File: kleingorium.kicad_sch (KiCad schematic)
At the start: 47 parts, among them J1 4017 Pins, J10 VCC, J11 GND, J12 4046 Comp In, J13 Select, J14 Input, J15 4046 SigIn, J16 4046 Comp, J17 Output, J18 4046 Comp In, J19 4046 Out, J2 4040 Output, J20 4040 Input, J21 4040 Output, J22 4017 Pins, J23 VCC, J24 GND, J3 4040 Input, J4 4046 Out, J5 4046 Comp, J6 Select, J7 Output, J8 Input, J9 4046 SigIn, Q1 2N3904, Q2 2N3904, Q3 2N3904, Q4 2N3904, Q5 2N3904, Q6 2N3904, SW1 4017 Feedback, SW2 4046 CompIn, SW3 Chain, SW4 4017 Feedback, SW5 4046 CompIn

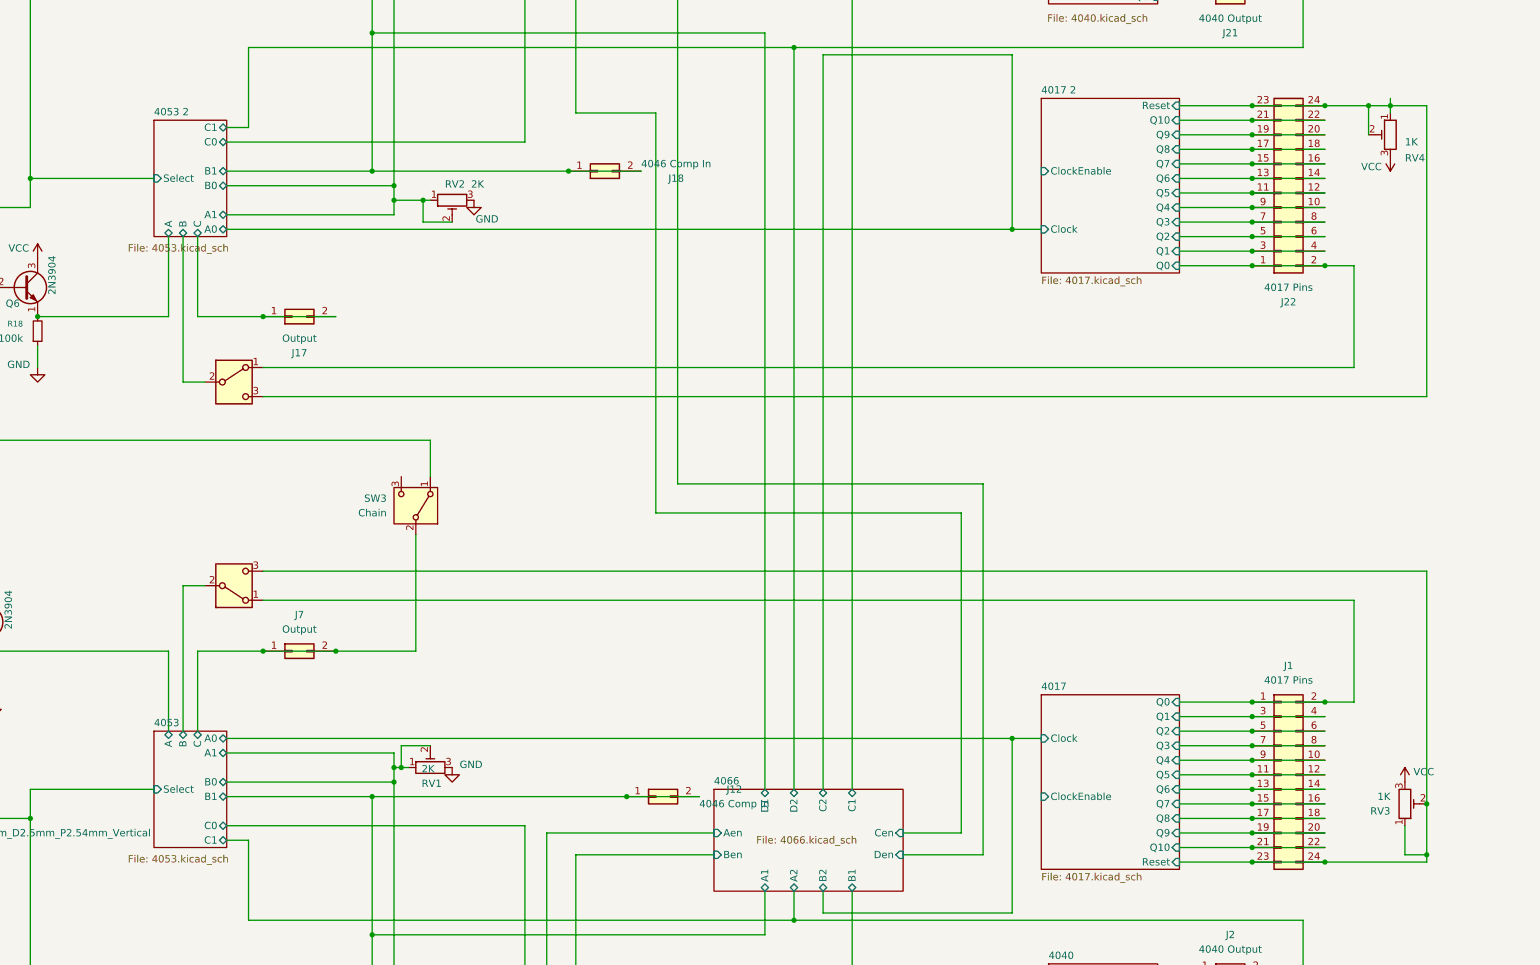
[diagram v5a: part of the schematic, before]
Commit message: add Inhibit 4046
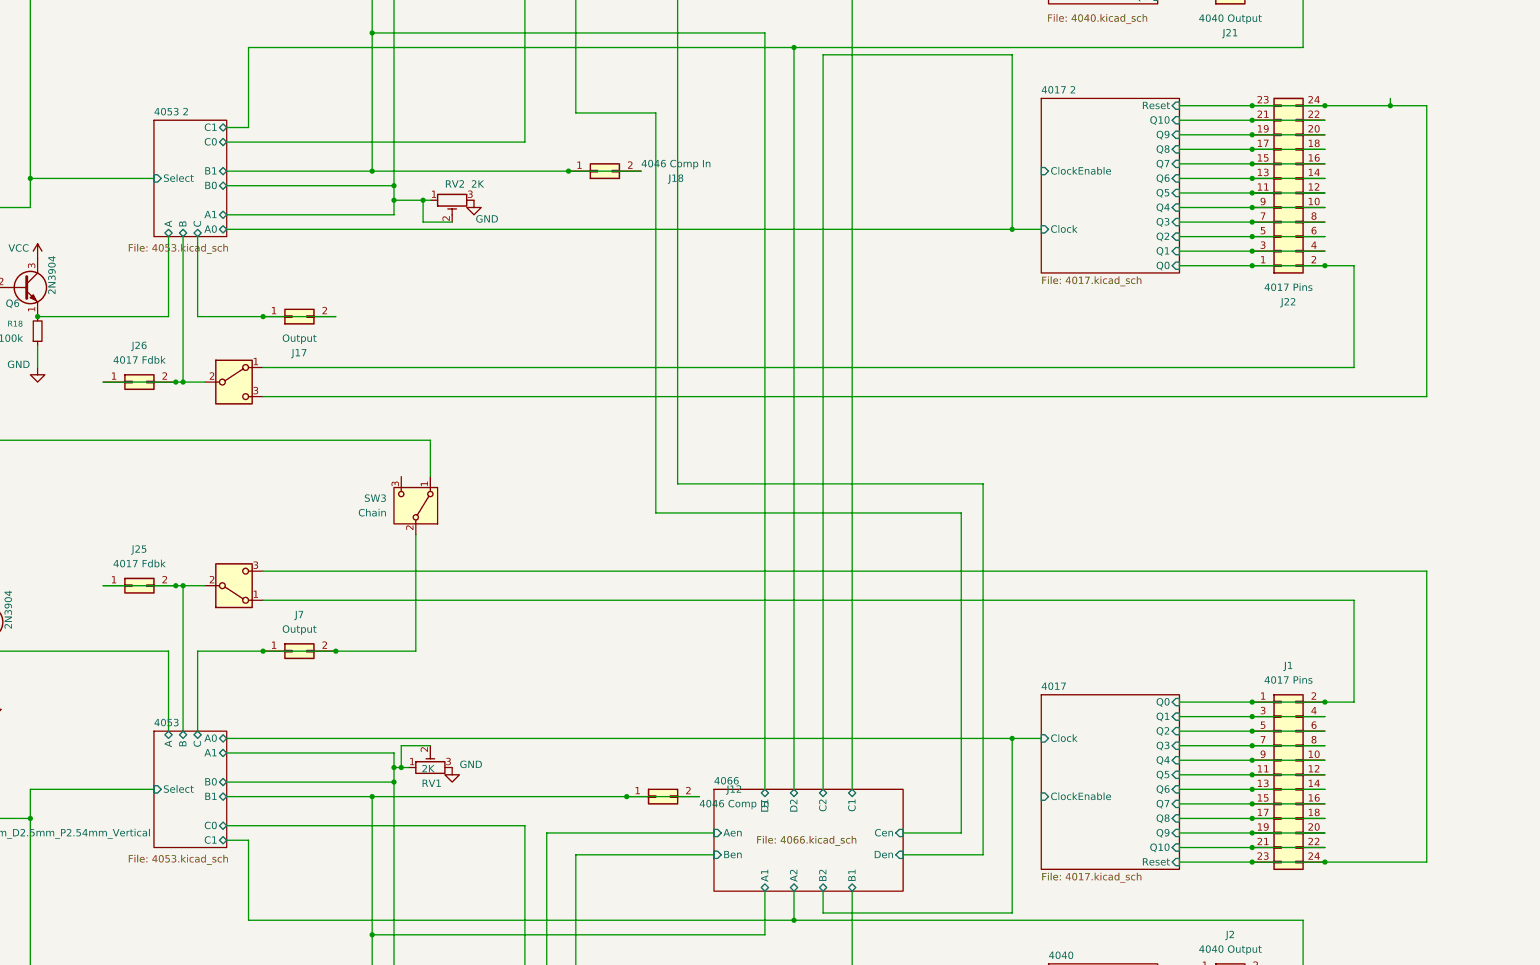
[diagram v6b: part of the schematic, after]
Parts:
- removed RV3, RV4: 1K, Potentiometer_THT:Potentiometer_Bourns_3296W_Vertical, symbol Device:R_Potentiometer_Trim
- added J25, J26: 4017 Fdbk, Connector_PinHeader_2.54mm:PinHeader_2x01_P2.54mm_Vertical, symbol Connector_Generic:Conn_02x01
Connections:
- net 4053 2/B: now also J26.1 (Pin_1), J26.2 (Pin_2)
- net 4053/B: now also J25.1 (Pin_1), J25.2 (Pin_2)

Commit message: v2 initial commit
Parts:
- removed J1, J22: 4017 Pins, Connector_PinHeader_2.54mm:PinHeader_2x12_P2.54mm_Vertical, symbol Connector_Generic:Conn_02x12_Odd_Even
- removed J12, J18: 4046 Comp In, Connector_PinHeader_2.54mm:PinHeader_2x01_P2.54mm_Vertical, symbol Connector_Generic:Conn_02x01
- removed J13, J6: Select, Connector_PinHeader_2.54mm:PinHeader_2x01_P2.54mm_Vertical, symbol Connector_Generic:Conn_02x01
- removed J14, J8: Input, Connector_PinHeader_2.54mm:PinHeader_2x01_P2.54mm_Vertical, symbol Connector_Generic:Conn_02x01
- removed J15, J9: 4046 SigIn, Connector_PinHeader_2.54mm:PinHeader_2x01_P2.54mm_Vertical, symbol Connector_Generic:Conn_02x01
- removed J16, J5: 4046 Comp, Connector_PinHeader_2.54mm:PinHeader_2x01_P2.54mm_Vertical, symbol Connector_Generic:Conn_02x01
- removed J17, J7: Output, Connector_PinHeader_2.54mm:PinHeader_2x01_P2.54mm_Vertical, symbol Connector_Generic:Conn_02x01
- removed J19, J4: 4046 Out, Connector_PinHeader_2.54mm:PinHeader_2x01_P2.54mm_Vertical, symbol Connector_Generic:Conn_02x01
- removed J2, J21: 4040 Output, Connector_PinHeader_2.54mm:PinHeader_2x12_P2.54mm_Vertical, symbol Connector_Generic:Conn_02x12_Odd_Even
- removed J20, J3: 4040 Input, Connector_PinHeader_2.54mm:PinHeader_1x02_P2.54mm_Vertical, symbol Connector_Generic:Conn_01x02
- removed J25, J26: 4017 Fdbk, Connector_PinHeader_2.54mm:PinHeader_2x01_P2.54mm_Vertical, symbol Connector_Generic:Conn_02x01
- removed Q1, Q2, Q3, Q4, Q5, Q6: 2N3904, Package_TO_SOT_THT:TO-92_Inline_Wide, symbol Transistor_BJT:2N3904
- removed R11, R14: 2.2k, Resistor_THT:R_Axial_DIN0207_L6.3mm_D2.5mm_P10.16mm_Horizontal, symbol Device:R_Small
- removed R12, R13: 100k, Resistor_THT:R_Axial_DIN0207_L6.3mm_D2.5mm_P10.16mm_Horizontal, symbol Device:R_Small
- removed R15, R16, R17, R18: 100k, Resistor_THT:R_Axial_DIN0207_L6.3mm_D2.5mm_P2.54mm_Vertical, symbol Device:R_Small
- removed RV1, RV2: 2K, Potentiometer_THT:Potentiometer_Bourns_3296W_Vertical, symbol Device:R_Potentiometer_Trim
- removed SW1, SW4: 4017 Feedback, Button_Switch_THT:SW_CK_JS202011CQN_DPDT_Straight, symbol Switch:SW_DPDT_x2
- removed SW2, SW5: 4046 CompIn, Button_Switch_THT:SW_E-Switch_EG1271_SPDT, symbol Switch:SW_SPDT
- removed SW3: Chain, Button_Switch_THT:SW_E-Switch_EG1271_SPDT, symbol Switch:SW_SPDT
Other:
- removed sheet 4017
- removed sheet 4017 2
- removed sheet 4040
- removed sheet 4040 2
- removed sheet 4046
- removed sheet 4046 2
- removed sheet 4053
- removed sheet 4053 2
- removed sheet 4066
- added sheet Multiplier-Divider (multiplier_divider.kicad_sch)

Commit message: schematic finished
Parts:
- renumbered J10 to J1, J23 to J2, J11 to J3, J24 to J4
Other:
- removed sheet utilities
- added sheet Bottom plate (bottom_plate.kicad_sch)
- added sheet Top Plate (top_plate.kicad_sch)
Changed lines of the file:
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@@
 	(paper "A3")
 	(junction
-		(at 370.84 185.42)
-		(diameter 0)
-		(color 0 0 0 0)
-	)
-	(junction
 		(at 386.08 182.88)
 		(diameter 0)
@@
 	)
 	(junction
-		(at 386.08 185.42)
+		(at 400.05 182.88)
+		(diameter 0)
+		(color 0 0 0 0)
+	)
+	(junction
+		(at 387.35 182.88)
+		(diameter 0)
+		(color 0 0 0 0)
+	)
+	(junction
+		(at 387.35 199.39)
 		(diameter 0)
 		(color 0 0 0 0)
@@
 	(wire
 		(pts
-			(xy 386.08 182.88) (xy 386.08 185.42)
-		)
-		(stroke
-			(width 0)
-			(type default)
-		)
-	)
-	(wire
-		(pts
-			(xy 400.05 201.93) (xy 386.08 201.93)
+			(xy 387.35 199.39) (xy 400.05 199.39)
+		)
+		(stroke
+			(width 0)
+			(type default)
+		)
+	)
+	(wire
+		(pts
+			(xy 386.08 182.88) (xy 386.08 199.39)
+		)
+		(stroke
+			(width 0)
+			(type default)
+		)
+	)
+	(wire
+		(pts
+			(xy 400.05 182.88) (xy 401.32 182.88)
+		)
+		(stroke
+			(width 0)
+			(type default)
+		)
+	)
+	(wire
+		(pts
+			(xy 358.14 199.39) (xy 370.84 199.39)
 		)
 		(stroke
@@
 	(wire
 		(pts
-			(xy 370.84 201.93) (xy 370.84 199.39)
-		)
-		(stroke
-			(width 0)
-			(type default)
-		)
-	)
-	(wire
-		(pts
-			(xy 400.05 199.39) (xy 400.05 201.93)
-		)
-		(stroke
-			(width 0)
-			(type default)
-		)
-	)
-	(wire
-		(pts
-			(xy 386.08 201.93) (xy 386.08 199.39)
-		)
-		(stroke
-			(width 0)
-			(type default)
-		)
-	)
-	(wire
-		(pts
-			(xy 400.05 182.88) (xy 400.05 185.42)
-		)
-		(stroke
-			(width 0)
-			(type default)
-		)
-	)
-	(wire
-		(pts
-			(xy 358.14 201.93) (xy 370.84 201.93)
+			(xy 400.05 182.88) (xy 387.35 182.88)
+		)
+		(stroke
+			(width 0)
+			(type default)
+		)
+	)
+	(wire
+		(pts
+			(xy 387.35 182.88) (xy 386.08 182.88)
 		)
 		(stroke
@@
 	(wire
 		(pts
-			(xy 400.05 185.42) (xy 386.08 185.42)
+			(xy 387.35 199.39) (xy 386.08 199.39)
 		)
 		(stroke
@@
 	(wire
 		(pts
-			(xy 386.08 185.42) (xy 386.08 199.39)
-		)
-		(stroke
-			(width 0)
-			(type default)
-		)
-	)
-	(wire
-		(pts
-			(xy 386.08 182.88) (xy 387.35 182.88)
-		)
-		(stroke
-			(width 0)
-			(type default)
-		)
-	)
-	(wire
-		(pts
-			(xy 358.14 182.88) (xy 358.14 185.42)
-		)
-		(stroke
-			(width 0)
-			(type default)
-		)
-	)
-	(wire
-		(pts
-			(xy 370.84 182.88) (xy 370.84 185.42)
-		)
-		(stroke
-			(width 0)
-			(type default)
-		)
-	)
-	(wire
-		(pts
-			(xy 358.14 199.39) (xy 358.14 201.93)
-		)
-		(stroke
-			(width 0)
-			(type default)
-		)
-	)
-	(wire
-		(pts
-			(xy 370.84 185.42) (xy 370.84 199.39)
+			(xy 370.84 182.88) (xy 370.84 199.39)
 		)
 		(stroke
@@
 	(wire
 		(pts
-			(xy 358.14 185.42) (xy 370.84 185.42)
-		)
-		(stroke
-			(width 0)
-			(type default)
-		)
-	)
-	(wire
-		(pts
-			(xy 386.08 199.39) (xy 387.35 199.39)
+			(xy 358.14 182.88) (xy 370.84 182.88)
 		)
 		(stroke
@@
 		(dnp no)
 		(fields_autoplaced yes)
-		(property "Reference" "J10"
+		(property "Reference" "J1"
 			(at 364.49 176.53 0)
 			(effects
@@
 			(project "kleingorium"
 				(path "/01c1f2c1-4d06-4880-847a-9ab55552e3fd"
-					(reference "J10")
+					(reference "J1")
 					(unit 1)
 				)
@@
 		(on_board yes)
 		(dnp no)
-		(property "Reference" "J24"
+		(property "Reference" "J4"
 			(at 393.7 193.04 0)
 			(effects
@@
 			(project "kleingorium"
 				(path "/01c1f2c1-4d06-4880-847a-9ab55552e3fd"
-					(reference "J24")
+					(reference "J4")
 					(unit 1)
 				)
@@
 		(dnp no)
 		(fields_autoplaced yes)
-		(property "Reference" "J23"
+		(property "Reference" "J2"
 			(at 364.49 193.04 0)
 			(effects
@@
 			(project "kleingorium"
 				(path "/01c1f2c1-4d06-4880-847a-9ab55552e3fd"
-					(reference "J23")
+					(reference "J2")
 					(unit 1)
 				)
@@
 		(on_board yes)
 		(dnp no)
-		(property "Reference" "J11"
+		(property "Reference" "J3"
 			(at 393.7 176.53 0)
 			(effects
@@
 			(project "kleingorium"
 				(path "/01c1f2c1-4d06-4880-847a-9ab55552e3fd"
-					(reference "J11")
+					(reference "J3")
 					(unit 1)
 				)
@@
 	)
 	(sheet
-		(at 330.2 179.07)
-		(size 12.7 3.81)
-		(exclude_from_sim no)
-		(in_bom yes)
-		(on_board yes)
-		(dnp no)
+		(at 290.83 181.61)
+		(size 22.86 19.05)
+		(exclude_from_sim no)
+		(in_bom yes)
+		(on_board yes)
+		(dnp no)
+		(fields_autoplaced yes)
 		(stroke
 			(width 0.1524)
@@
 			(color 0 0 0 0.0000)
 		)
-		(property "Sheetname" "utilities"
-			(at 330.2 178.3584 0)
+		(property "Sheetname" "Top Plate"
+			(at 290.83 180.8984 0)
 			(effects
 				(font
@@
 			)
 		)
-		(property "Sheetfile" "utilities.kicad_sch"
-			(at 331.724 184.404 0)
+		(property "Sheetfile" "top_plate.kicad_sch"
+			(at 290.83 201.2446 0)
 			(effects
 				(font
@@
 	)
 	(sheet
-		(at 39.37 257.81)
+		(at 245.11 175.26)
 		(size 19.05 15.24)
 		(exclude_from_sim no)
@@
 		)
 		(property "Sheetname" "Multiplier-Divider"
-			(at 39.37 257.0984 0)
+			(at 245.11 174.5484 0)
 			(effects
 				(font
@@
 		)
 		(property "Sheetfile" "multiplier_divider.kicad_sch"
-			(at 39.37 273.6346 0)
+			(at 245.11 191.0846 0)
 			(effects
 				(font
@@
 			(project "kleingorium"
 				(path "/01c1f2c1-4d06-4880-847a-9ab55552e3fd"
-					(page "13")
-				)
-			)
+					(page "2")
+				)
+			)
+		)
+	)
+	(sheet
+		(at 290.83 210.82)
+		(size 26.67 20.32)
+		(exclude_from_sim no)
+		(in_bom yes)
+		(on_board yes)
+		(dnp no)
+		(fields_autoplaced yes)
+		(stroke
+			(width 0.1524)
+			(type solid)
+		)
+		(fill
+			(color 0 0 0 0.0000)
+		)
+		(property "Sheetname" "Bottom plate"
+			(at 290.83 210.1084 0)
+			(effects
+				(font
+					(size 1.27 1.27)
+				)
+				(justify left bottom)
+			)
+		)
+		(property "Sheetfile" "bottom_plate.kicad_sch"
+			(at 290.83 231.7246 0)
+			(effects
+				(font
+					(size 1.27 1.27)
+				)
+				(justify left top)
+			)
+		)
+		(instances
+			(project "kleingorium"
+				(path "/01c1f2c1-4d06-4880-847a-9ab55552e3fd"
+					(page "14")
+				)
+			)
